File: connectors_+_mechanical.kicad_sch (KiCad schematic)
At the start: 51 parts, among them J1 Motor0, J10 USB_C_Receptacle_USB2.0_14P, J2 Motor1, J3 Battery Input, J5 Conn_01x04, J6 Conn_01x04, Q1 BSP613P, U7 INA180A1

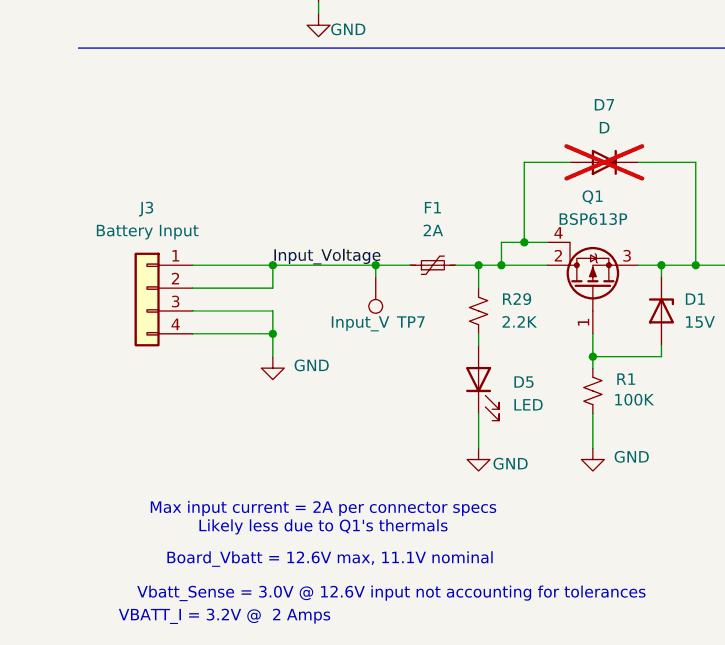
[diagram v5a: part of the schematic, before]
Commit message: CBjamo updats
Added J11 to accommodate batteries on both sides and changed pinout of J8 to have ground in the middle.
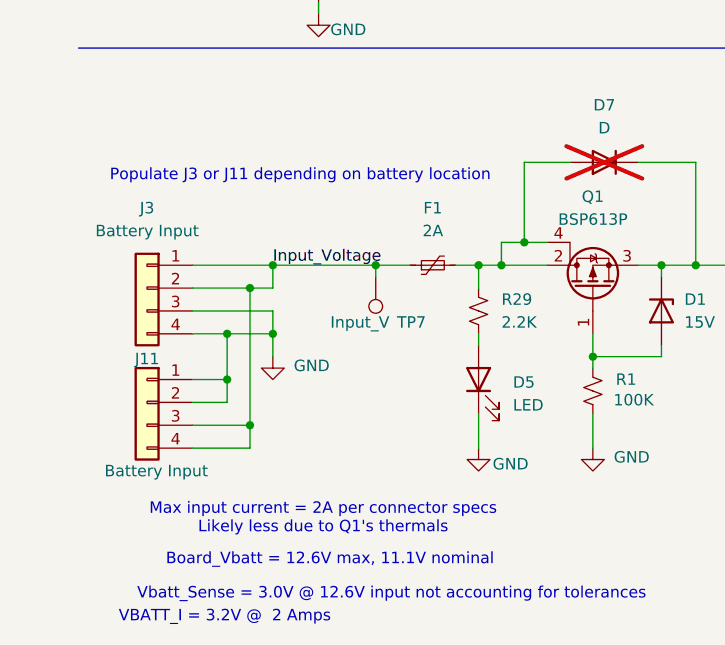
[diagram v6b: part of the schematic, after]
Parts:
- added J11: Battery Input, Connector_JST:JST_SH_BM04B-SRSS-TB_1x04-1MP_P1.00mm_Vertical, symbol Connector_Generic:Conn_01x04
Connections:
- net GND: now also J11.1 (Pin_1), J11.2 (Pin_2)
- net Input_Voltage: now also J11.3 (Pin_3), J11.4 (Pin_4)
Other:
- note added: "Populate J3 or J11 depending on battery location"
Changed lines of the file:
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@@
 	)
 	(junction
+		(at 31.75 132.08)
+		(diameter 0)
+		(color 0 0 0 0)
+	)
+	(junction
 		(at 59.69 129.54)
 		(diameter 0)
@@
 	)
 	(junction
+		(at 31.75 147.32)
+		(diameter 0)
+		(color 0 0 0 0)
+	)
+	(junction
 		(at 39.37 69.85)
 		(diameter 0)
@@
 	)
 	(junction
+		(at 29.21 142.24)
+		(diameter 0)
+		(color 0 0 0 0)
+	)
+	(junction
 		(at 238.76 129.54)
 		(diameter 0)
@@
 	)
 	(junction
+		(at 29.21 137.16)
+		(diameter 0)
+		(color 0 0 0 0)
+	)
+	(junction
 		(at 105.41 129.54)
 		(diameter 0)
@@
 	(wire
 		(pts
+			(xy 29.21 142.24) (xy 29.21 144.78)
+		)
+		(stroke
+			(width 0)
+			(type default)
+		)
+	)
+	(wire
+		(pts
 			(xy 88.9 129.54) (xy 105.41 129.54)
 		)
@@
 	(wire
 		(pts
+			(xy 25.4 149.86) (xy 31.75 149.86)
+		)
+		(stroke
+			(width 0)
+			(type default)
+		)
+	)
+	(wire
+		(pts
 			(xy 57.15 129.54) (xy 59.69 129.54)
 		)
@@
 	(wire
 		(pts
+			(xy 25.4 142.24) (xy 29.21 142.24)
+		)
+		(stroke
+			(width 0)
+			(type default)
+		)
+	)
+	(wire
+		(pts
 			(xy 151.13 57.15) (xy 154.94 57.15)
 		)
@@
 	(wire
 		(pts
+			(xy 31.75 132.08) (xy 31.75 147.32)
+		)
+		(stroke
+			(width 0)
+			(type default)
+		)
+	)
+	(wire
+		(pts
 			(xy 114.3 133.35) (xy 114.3 129.54)
 		)
@@
 	(wire
 		(pts
-			(xy 25.4 132.08) (xy 34.29 132.08)
+			(xy 25.4 132.08) (xy 31.75 132.08)
 		)
 		(stroke
@@
 		)
 	)
+	(wire
+		(pts
+			(xy 31.75 132.08) (xy 34.29 132.08)
+		)
+		(stroke
+			(width 0)
+			(type default)
+		)
+	)
 	(polyline
 		(pts
@@
 	(wire
 		(pts
+			(xy 25.4 144.78) (xy 29.21 144.78)
+		)
+		(stroke
+			(width 0)
+			(type default)
+		)
+	)
+	(wire
+		(pts
 			(xy 245.11 129.54) (xy 247.65 129.54)
 		)
@@
 	(wire
 		(pts
+			(xy 25.4 147.32) (xy 31.75 147.32)
+		)
+		(stroke
+			(width 0)
+			(type default)
+		)
+	)
+	(wire
+		(pts
 			(xy 266.7 157.48) (xy 262.89 157.48)
 		)
@@
 	(wire
 		(pts
+			(xy 31.75 147.32) (xy 31.75 149.86)
+		)
+		(stroke
+			(width 0)
+			(type default)
+		)
+	)
+	(wire
+		(pts
 			(xy 139.7 85.09) (xy 139.7 82.55)
 		)
@@
 	(wire
 		(pts
+			(xy 29.21 137.16) (xy 34.29 137.16)
+		)
+		(stroke
+			(width 0)
+			(type default)
+		)
+	)
+	(wire
+		(pts
 			(xy 116.84 33.02) (xy 152.4 33.02)
 		)
@@
 	(wire
 		(pts
+			(xy 29.21 137.16) (xy 29.21 142.24)
+		)
+		(stroke
+			(width 0)
+			(type default)
+		)
+	)
+	(wire
+		(pts
 			(xy 57.15 137.16) (xy 57.15 138.43)
 		)
@@
 	(wire
 		(pts
-			(xy 25.4 137.16) (xy 34.29 137.16)
+			(xy 25.4 137.16) (xy 29.21 137.16)
 		)
 		(stroke
@@
 		)
 	)
+	(text "Populate J3 or J11 depending on battery location\n"
+		(exclude_from_sim no)
+		(at 37.338 119.634 0)
+		(effects
+			(font
+				(size 1.27 1.27)
+			)
+		)
+	)
 	(text "Board_Vbatt = 12.6V max, 11.1V nominal"
 		(exclude_from_sim no)
@@
 					(unit 1)
 				)
+			)
+		)
+	)
+	(symbol
+		(lib_id "Connector_Generic:Conn_01x04")
+		(at 20.32 144.78 0)
+		(mirror y)
+		(unit 1)
+		(exclude_from_sim no)
+		(in_bom yes)
+		(on_board yes)
+		(dnp no)
+		(property "Reference" "J11"
+			(at 20.32 139.954 0)
+			(effects
+				(font
+					(size 1.27 1.27)
+				)
+			)
+		)
+		(property "Value" "Battery Input"
+			(at 21.336 152.4 0)
+			(effects
+				(font
+					(size 1.27 1.27)
+				)
+			)
+		)
+		(property "Footprint" "Connector_JST:JST_SH_BM04B-SRSS-TB_1x04-1MP_P1.00mm_Vertical"
+			(at 20.32 144.78 0)
+			(effects
+				(font
+					(size 1.27 1.27)
+				)
+				(hide yes)
+			)
+		)
+		(property "Datasheet" "~"
+			(at 20.32 144.78 0)
+			(effects
+				(font
+					(size 1.27 1.27)
+				)
+				(hide yes)
+			)
+		)
+		(property "Description" "Generic connector, single row, 01x04, script generated (kicad-library-utils/schlib/autogen/connector/)"
+			(at 20.32 144.78 0)
+			(effects
+				(font
+					(size 1.27 1.27)
+				)
+				(hide yes)
+			)
+		)
+		(pin "2"
+		)
+		(pin "1"
+		)
+		(pin "4"
+		)
+		(pin "3"
+		)
+		(instances
+			(project "moon_child"
+				(path "/9fe08eae-9310-46cf-b272-eac4209a7b3e/2020c3b7-5d3f-4410-b013-36b6a2638d7a"
+					(reference "J11")
+					(unit 1)
+				)

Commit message: Bom updates
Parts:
- C19: MPN (none) -> CL10B105KP8NNNC; Package (none) -> 0603
- D1: MPN (none) -> BZT52C15S-7-F; Package (none) -> SOD-323
- D11, D12, D13, D9: MPN (none) -> ESDA6V1BC6; Package (none) -> SOT-23-6
- D2: MPN (none) -> MBR0530T1G; Package (none) -> SOD-123
- D5, D6: MPN (none) -> LTST-C190KFKT; Package (none) -> 0603
- D7: MPN (none) -> S1J-13-F; Package (none) -> SMA; now fitted
- F1: MPN (none) -> MF-NSML200/12-2; Package (none) -> 1206
- F2: MPN (none) -> 0ZCJ0025FF2E; Package (none) -> 1206
- F5: MPN (none) -> 0ZCJ0050AF2E; Package (none) -> 1206
- FID1, FID2, FID3, FID4, FID5, FID6, J5, J6, TP11, TP12, TP13, TP14, TP15, TP16, TP18, TP19, TP21, TP22, TP24, TP25, TP7, TP8: now not fitted
- J1, J2: MPN (none) -> BM06B-SRSS-TB
- J10: MPN (none) -> USB4115-03-C
- J11, J3: MPN (none) -> BM04B-SRSS-TB
- Q1: MPN (none) -> BSP613PH6327XTSA1; Package (none) -> SOT223-4
- R1, R18: MPN (none) -> RC0402JR-07100KL; Package (none) -> 0402
- R17: value 320K -> 324K; MPN (none) -> RC0402FR-07324KL; Package (none) -> 0402
- R29, R30: MPN (none) -> RC0402JR-072K2L; Package (none) -> 0402
- R31: MPN (none) -> RL1206FR-070R08L; Package (none) -> 1206
- R42: MPN (none) -> RC0402JR-0710KL; Package (none) -> 0402
- R52, R53: Package (none) -> 0402
- U7: MPN (none) -> INA180A1IDBVR; Package (none) -> SOT-23-5

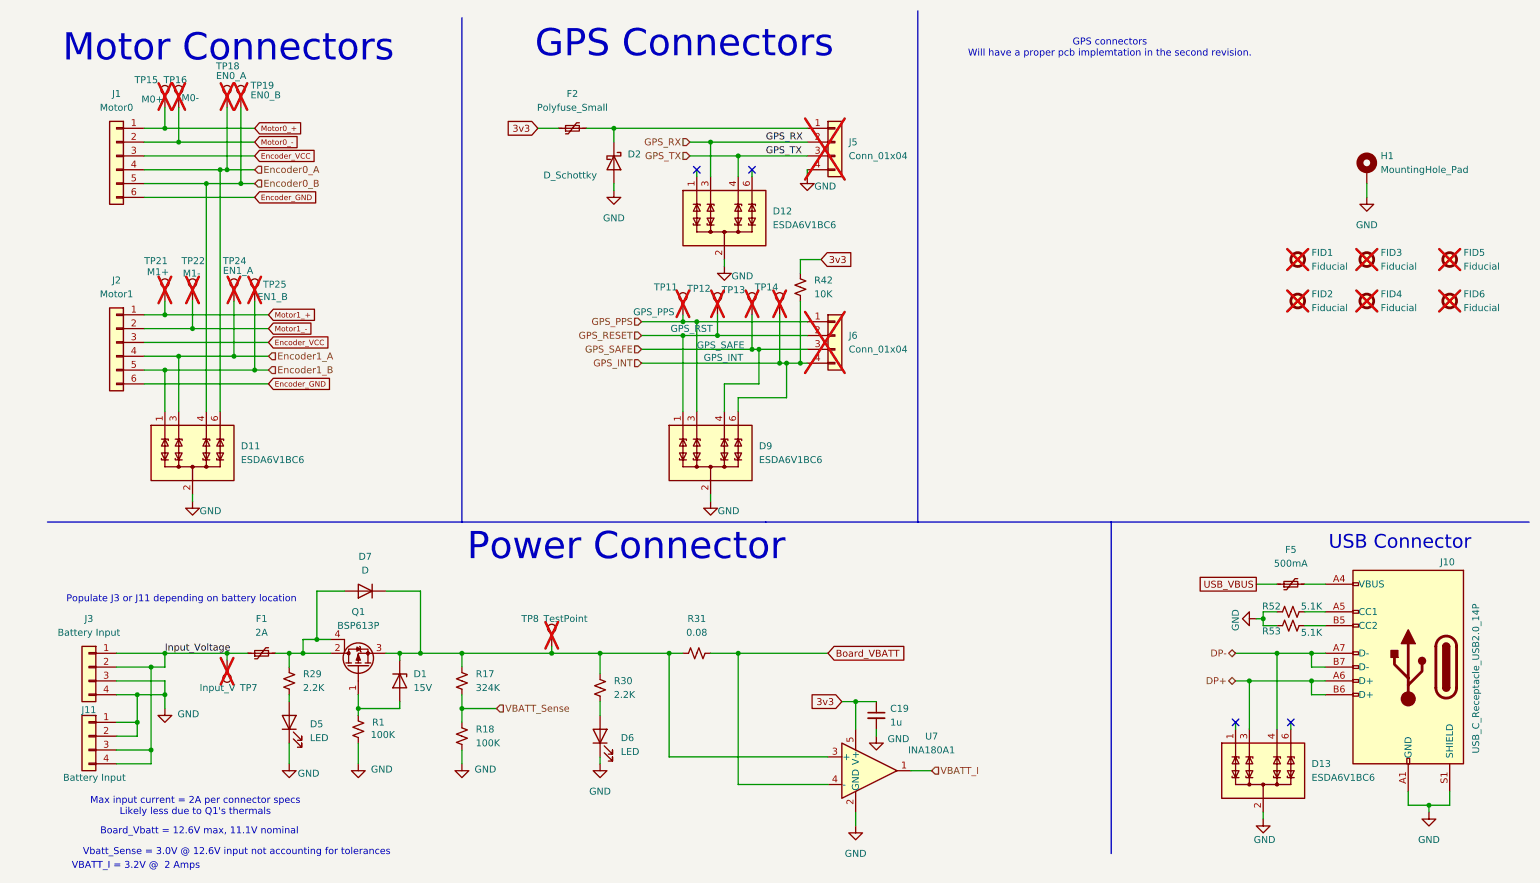
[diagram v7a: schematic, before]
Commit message: Launch day
Completed BOM, added silk art
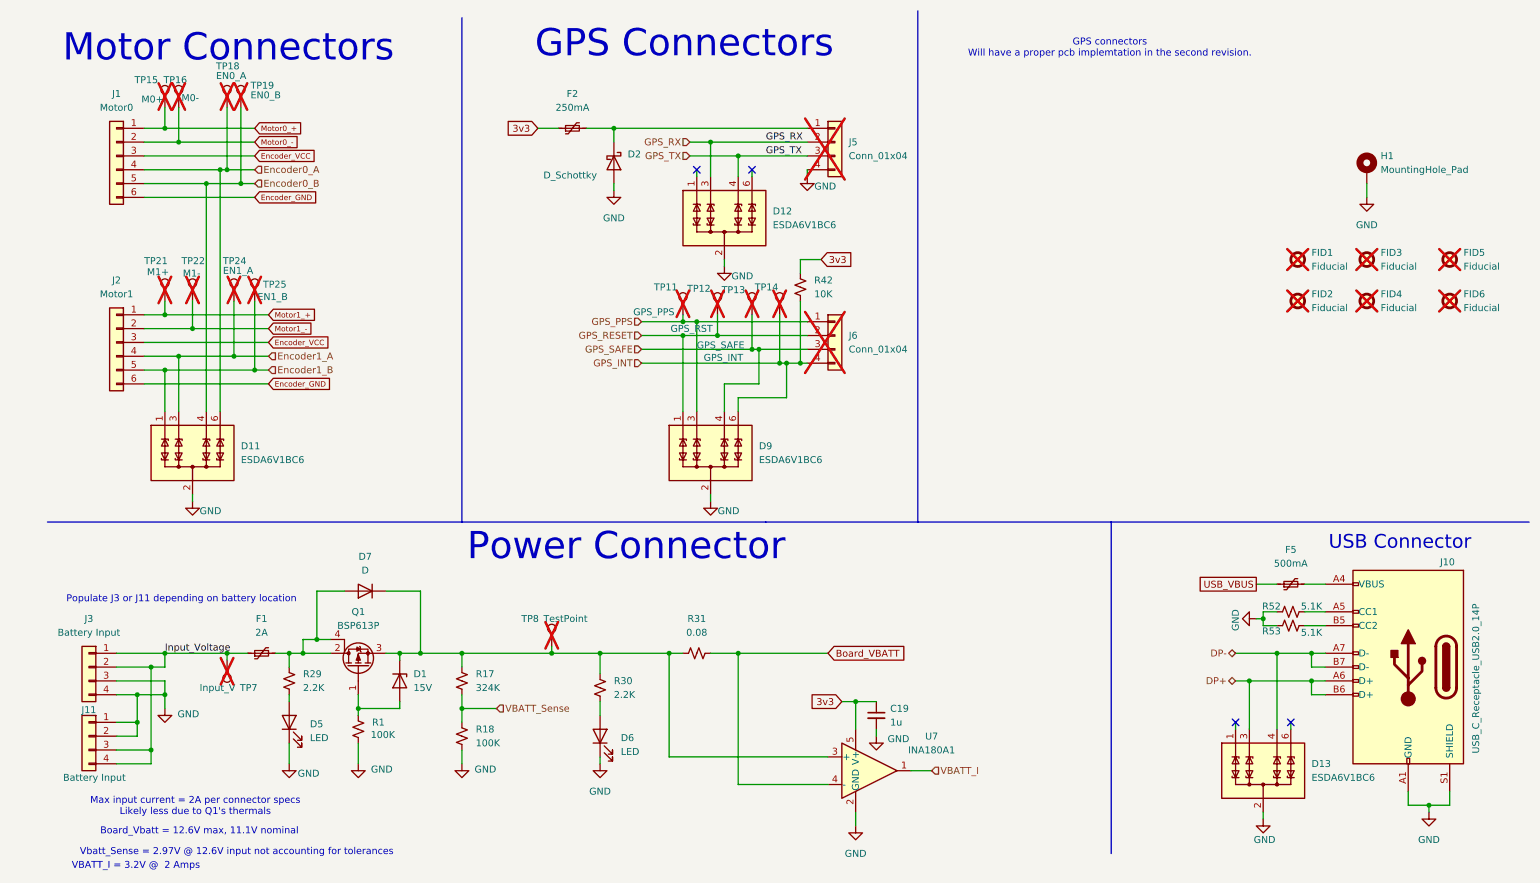
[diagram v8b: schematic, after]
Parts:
- F2: value Polyfuse_Small -> 250mA
- R52, R53: MPN (none) -> RC0402FR-075K1L
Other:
- note added: "Vbatt_Sense = 2.97V @ 12.6V input not accounting for tolerances"
- note removed: "Vbatt_Sense = 3.0V @ 12.6V input not accounting for tolerances"
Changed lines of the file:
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@@
 		)
 	)
-	(text "Vbatt_Sense = 3.0V @ 12.6V input not accounting for tolerances"
+	(text "Vbatt_Sense = 2.97V @ 12.6V input not accounting for tolerances"
 		(exclude_from_sim no)
 		(at 47.498 166.116 0)
@@
 			)
 		)
-		(property "Value" "Polyfuse_Small"
+		(property "Value" "250mA"
 			(at 109.22 29.21 90)
 			(effects
@@
 			)
 		)
+		(property "MPN" "RC0402FR-075K1L"
+			(at 241.3 121.92 0)
+			(effects
+				(font
+					(size 1.27 1.27)
+				)
+				(hide yes)
+			)
+		)
 		(pin "2"
 		)
@@
 			(at 241.3 124.46 0)
 			(effects
+				(font
+					(size 1.27 1.27)
+				)
+				(hide yes)
+			)
+		)
+		(property "MPN" "RC0402FR-075K1L"
+			(at 241.3 124.46 0)
+			(effects
